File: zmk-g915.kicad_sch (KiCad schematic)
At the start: 47 parts, among them J1 Prog_conn, J2 Tag connect TC2030-CTX, J3 53047-0460, SW1 Reset Switch, U1 nRF52840-QIAA-R/nRF52833-QIAA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, U2 SN74AHCT1G125, Y1 32.768kHz, Y2 32MHz

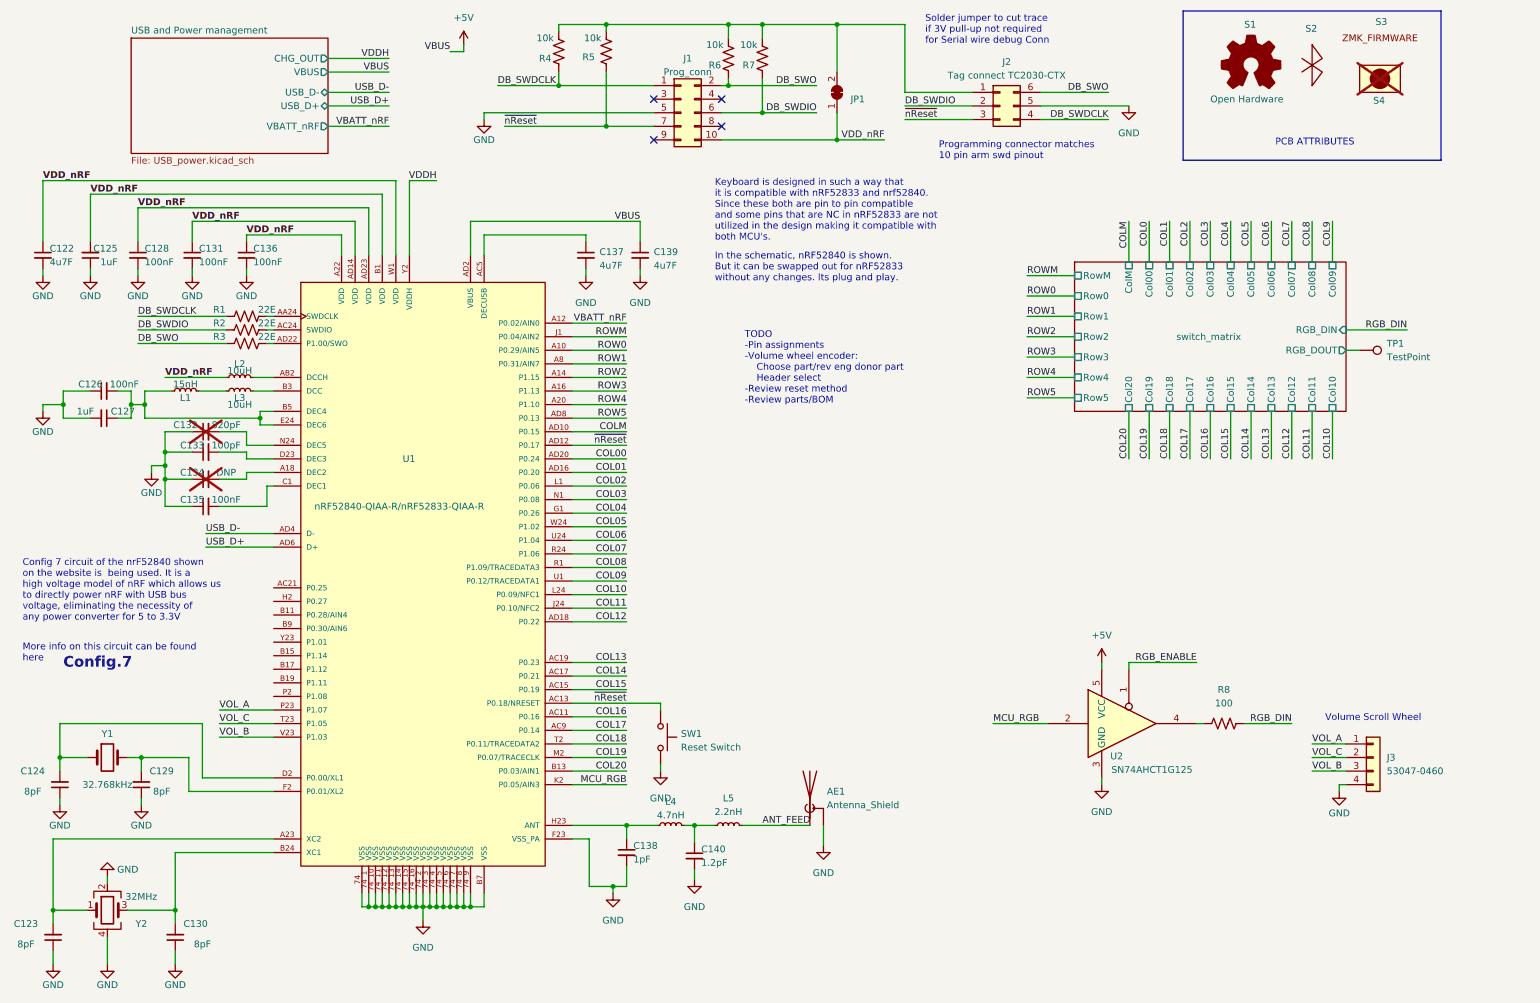
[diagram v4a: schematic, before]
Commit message: Status LEDs
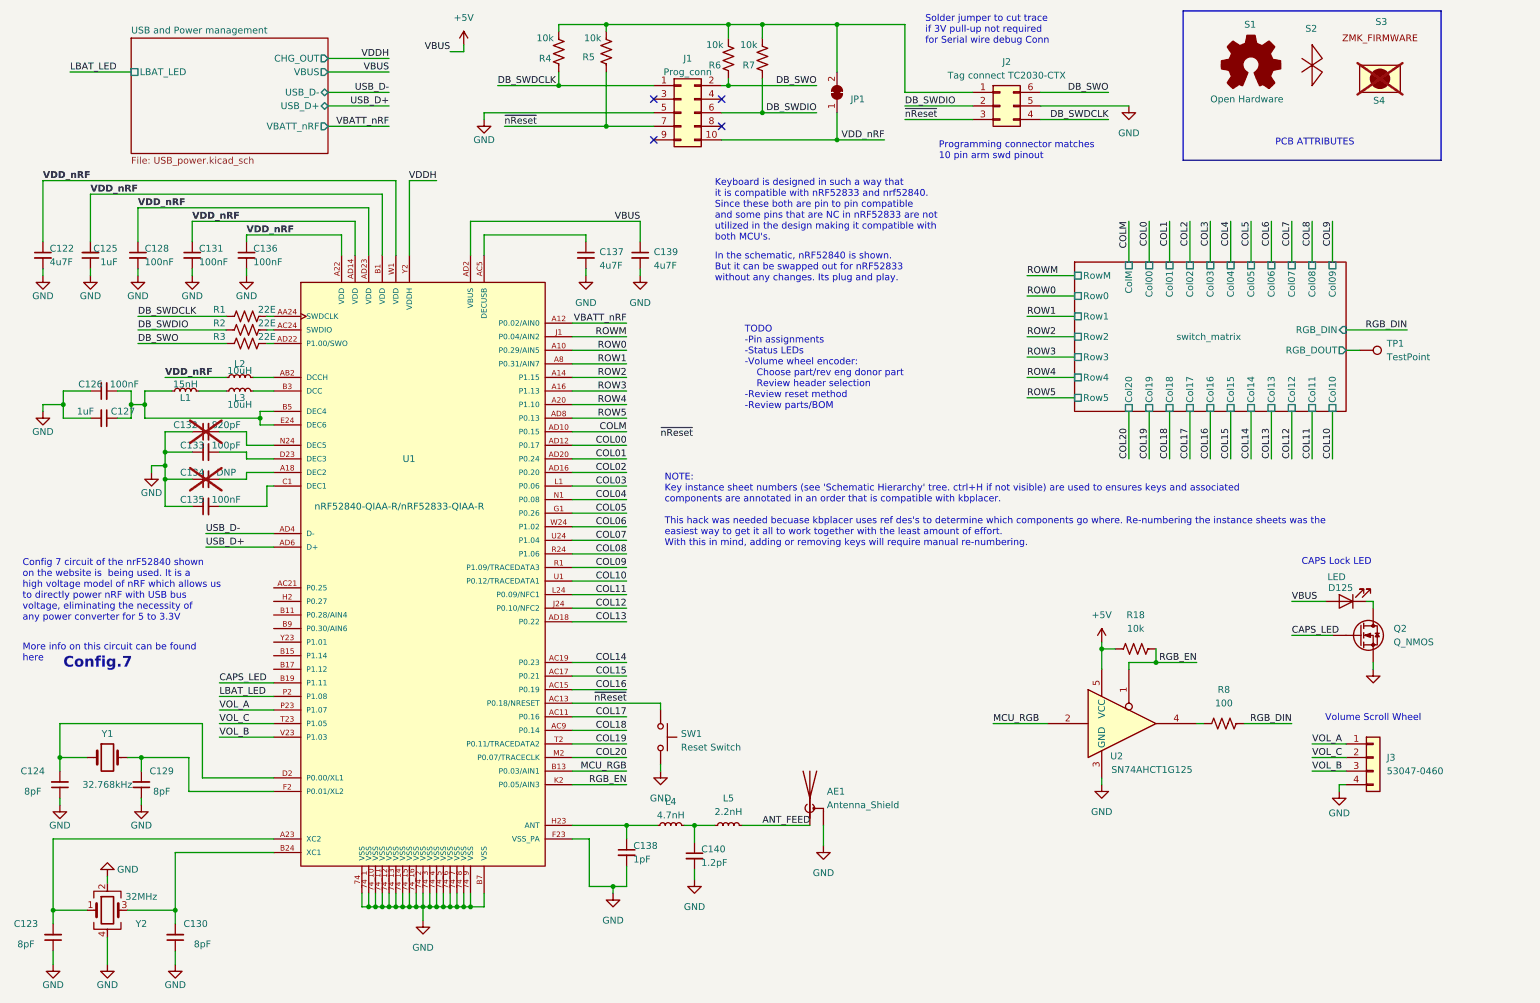
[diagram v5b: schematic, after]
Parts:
- added D125: LED, keyboard:LED_0603_1608Metric, symbol Device:LED
- added Q2: Q_NMOS, keyboard:SOT-23-3, symbol Device:Q_NMOS
- added R18: 10k, Resistor_SMD:R_0402_1005Metric, symbol keyboard:R_US
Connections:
- net +5V: now also D125.2 (A), R18.1
- net COL00: now also U1.AD12 (P0.17); no longer U1.AD20 (P0.24)
- net COL01: now also U1.AD20 (P0.24); no longer U1.AD16 (P0.20)
- net COL02: now also U1.AD16 (P0.20); no longer U1.L1 (P0.06)
- net COL03: now also U1.L1 (P0.06); no longer U1.N1 (P0.08)
- net COL04: now also U1.N1 (P0.08); no longer U1.G1 (P0.26)
- net COL05: now also U1.G1 (P0.26); no longer U1.W24 (P1.02)
- net COL06: now also U1.W24 (P1.02); no longer U1.U24 (P1.04)
- net COL07: now also U1.U24 (P1.04); no longer U1.R24 (P1.06)
- net COL08: now also U1.R24 (P1.06); no longer U1.R1 (P1.09/TRACEDATA3)
- net COL09: now also U1.R1 (P1.09/TRACEDATA3); no longer U1.U1 (P0.12/TRACEDATA1)
- net COL10: now also U1.U1 (P0.12/TRACEDATA1); no longer U1.L24 (P0.09/NFC1)
- net COL11: now also U1.L24 (P0.09/NFC1); no longer U1.J24 (P0.10/NFC2)
- net COL12: now also U1.J24 (P0.10/NFC2); no longer U1.AD18 (P0.22)
- net COL13: now also U1.AD18 (P0.22); no longer U1.AC19 (P0.23)
- net COL14: now also U1.AC19 (P0.23); no longer U1.AC17 (P0.21)
- net COL15: now also U1.AC17 (P0.21); no longer U1.AC15 (P0.19)
- net COL16: now also U1.AC15 (P0.19); no longer U1.AC11 (P0.16)
- net COL17: now also U1.AC11 (P0.16); no longer U1.AC9 (P0.14)
- net COL18: now also U1.AC9 (P0.14); no longer U1.T2 (P0.11/TRACEDATA2)
- net COL19: now also U1.T2 (P0.11/TRACEDATA2); no longer U1.M2 (P0.07/TRACECLK)
- net COL20: now also U1.M2 (P0.07/TRACECLK); no longer U1.B13 (P0.03/AIN1)
- net GND: now also Q2.S
- net MCU_RGB: now also U1.B13 (P0.03/AIN1); no longer U1.K2 (P0.05/AIN3)
- net ~{nReset}: no longer U1.AD12 (P0.17)
- net CAPS_LED: now reaches U1.B19 (P1.11)
- net CAPS_LED: now also Q2.G
- net LBAT_LED: now reaches U1.P2 (P1.08)
- net RGB_ENABLE renamed RGB_EN
- net RGB_EN: now also U1.K2 (P0.05/AIN3), R18.2
- new net: D125.1 (K), Q2.D
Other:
- sheet USB and Power management ports: added LBAT_LED; removed none
- note added: "CAPS Lock LED"
- note added: "NOTE: Key instance sheet numbers (see 'Schematic Hierarchy' tree. ctrl+H if not visible) are used to ensures keys and associated components are annotated in an order that is compatible with kbplacer. This hack was needed becuase kbplacer uses ref des's to determine which components go where. Re-numbering the instance sheets was the easiest way to get it all to work together with the least amount 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"
- note added: "TODO -Pin assignments -Status LEDs -Volume wheel encoder: Choose part/rev eng donor part Review header selection -Review reset method -Review parts/BOM"
- note removed: "TODO -Pin assignments -Volume wheel encoder: Choose part/rev eng donor part Header select -Review reset method -Review parts/BOM"

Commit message: Status LED work
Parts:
- added R20: R_US, keyboard:R_0402_1005Metric, symbol keyboard:R_US
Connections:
- net +5V: now also R20.2; no longer D125.2 (A)
- new net: D125.2 (A), R20.1
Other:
- note added: "TODO -Pin assignments -Status LEDs -Volume wheel encoder: Choose part/rev eng donor part Review header selection -Review reset necessity/method -Review parts/BOM -USB-C PD?? space dev/debug effort"
- note removed: "TODO -Pin assignments -Status LEDs -Volume wheel encoder: Choose part/rev eng donor part Review header selection -Review reset method -Review parts/BOM"
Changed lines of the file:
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@@
 		)
 	)
-	(text "TODO\n-Pin assignments\n-Status LEDs\n-Volume wheel encoder:\n	Choose part/rev eng donor part\n	Review header selection\n-Review reset method\n-Review parts/BOM"
+	(text "TODO\n-Pin assignments\n-Status LEDs\n-Volume wheel encoder:\n	Choose part/rev eng donor part\n	Review header selection\n-Review reset necessity/method\n-Review parts/BOM\n-USB-C PD??\n	space\n	dev/debug effort"
 		(exclude_from_sim no)
 		(at 151.638 80.772 0)
@@
 	(wire
 		(pts
-			(xy 254 124.46) (xy 260.35 124.46)
+			(xy 245.11 124.46) (xy 251.46 124.46)
 		)
 		(stroke
@@
 	(wire
 		(pts
+			(xy 259.08 124.46) (xy 260.35 124.46)
+		)
+		(stroke
+			(width 0)
+			(type default)
+		)
+	)
+	(wire
+		(pts
 			(xy 43.18 96.52) (xy 43.18 99.06)
 		)
@@
 	)
 	(label "VBUS"
-		(at 254 124.46 0)
+		(at 245.11 124.46 0)
 		(effects
 			(font
@@
 					(unit 1)
 				)
+			)
+		)
+	)
+	(symbol
+		(lib_id "keyboard:R_US")
+		(at 255.27 124.46 0)
+		(unit 1)
+		(exclude_from_sim no)
+		(in_bom yes)
+		(on_board yes)
+		(dnp no)
+		(property "Reference" "R20"
+			(at 255.27 121.92 0)
+			(effects
+				(font
+					(size 1.27 1.27)
+				)
+			)
+		)
+		(property "Value" "R_US"
+			(at 255.27 127 0)
+			(effects
+				(font
+					(size 1.27 1.27)
+				)
+			)
+		)
+		(property "Footprint" "keyboard:R_0402_1005Metric"
+			(at 255.016 125.476 0)
+			(effects
+				(font
+					(size 1.27 1.27)
+				)
+				(hide yes)
+			)
+		)
+		(property "Datasheet" "https://datasheet.lcsc.com/lcsc/2304140030_YAGEO-RC0402FR-071K2L_C138040.pdf"
+			(at 255.27 124.46 90)
+			(effects
+				(font
+					(size 1.27 1.27)
+				)
+				(hide yes)
+			)
+		)
+		(property "Description" ""
+			(at 255.27 124.46 0)
+			(effects
+				(font
+					(size 1.27 1.27)
+				)
+				(hide yes)
+			)
+		)
+		(property "PN" "RC0402FR-071K2L"
+			(at 255.27 124.46 0)
+			(effects
+				(font
+					(size 1.27 1.27)
+				)
+				(hide yes)
+			)
+		)
+		(property "LCSC Part Number" "C138040"
+			(at 255.27 124.46 0)
+			(effects
+				(font
+					(size 1.27 1.27)
+				)
+				(hide yes)
+			)
+		)
+		(property "LCSC link" "https://www.lcsc.com/product-detail/Chip-Resistor-Surface-Mount_YAGEO-RC0402FR-071K2L_C138040.html"
+			(at 255.27 124.46 0)
+			(effects
+				(font
+					(size 1.27 1.27)
+				)
+				(hide yes)
+			)
+		)
+		(pin "1"
+		)
+		(pin "2"
+		)
+		(instances
+			(project "zmk-g915"
+				(path "/ef112b03-6536-453f-8127-17d1495b48aa"
+					(reference "R20")
+					(unit 1)
+				)

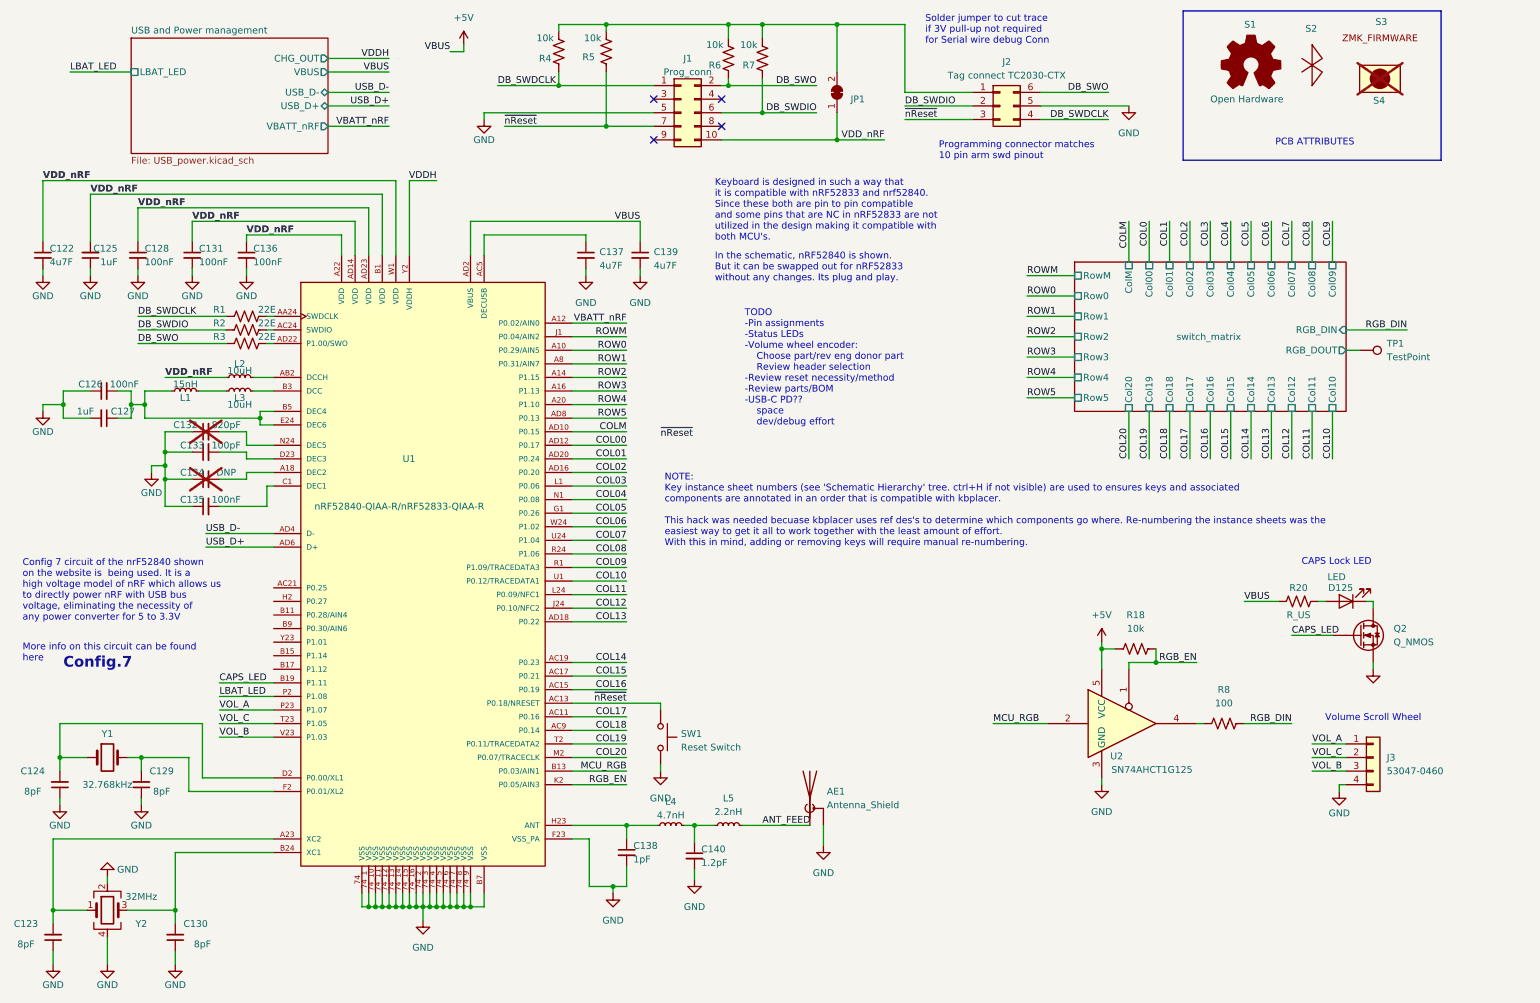
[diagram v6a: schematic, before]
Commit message: Minor sch changes. Work towards matching g915 pcb dimensions
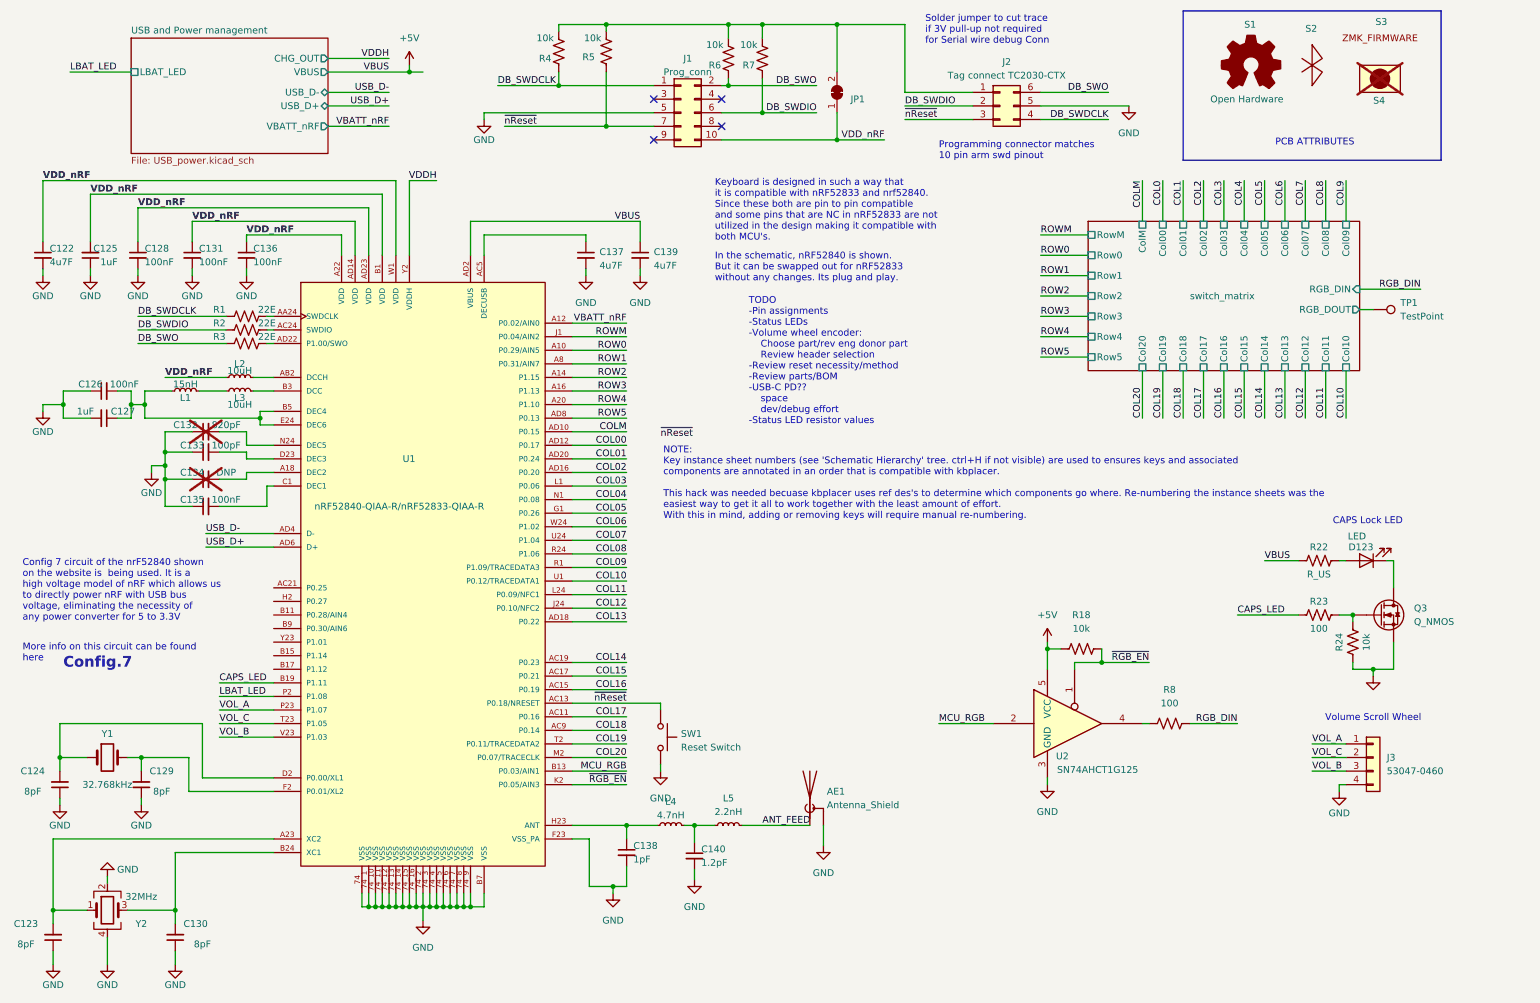
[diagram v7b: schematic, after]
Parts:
- removed D125: LED, keyboard:LED_0603_1608Metric, symbol Device:LED
- removed Q2: Q_NMOS, keyboard:SOT-23-3, symbol Device:Q_NMOS
- removed R20: R_US, keyboard:R_0402_1005Metric, symbol keyboard:R_US
- added D123: LED, keyboard:LED_0603_1608Metric, symbol Device:LED
- added Q3: Q_NMOS, keyboard:SOT-23-3, symbol Device:Q_NMOS
- added R22: R_US, keyboard:R_0402_1005Metric, symbol keyboard:R_US
- added R23: 100, keyboard:R_0402_1005Metric, symbol keyboard:R_US
- added R24: 10k, keyboard:R_0402_1005Metric, symbol keyboard:R_US
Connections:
- net +5V: now also R22.2
- net CAPS_LED: now also R23.2
- net GND: now also Q3.S, R24.2
- net RGB_EN renamed ~{RGB_EN}
- new net: Q3.G, R23.1, R24.1
- new net: D123.1 (K), Q3.D
- new net: D123.2 (A), R22.1
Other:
- note added: "TODO -Pin assignments -Status LEDs -Volume wheel encoder: Choose part/rev eng donor part Review header selection -Review reset necessity/method -Review parts/BOM -USB-C PD?? space dev/debug effort -Status LED resistor values"
- note removed: "TODO -Pin assignments -Status LEDs -Volume wheel encoder: Choose part/rev eng donor part Review header selection -Review reset necessity/method -Review parts/BOM -USB-C PD?? space dev/debug effort"
- moved on the sheet: R18, R8, TP1, U2

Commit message: Power supply and PCB stuff
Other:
- note added: "TODO -Pin assignments -Status LEDs -Volume wheel encoder: Choose part/rev eng donor part Review header selection -Review reset necessity/method -Review parts/BOM -USB-C PD?? No real benefit. Battery capcaity is low so max charging current is low. -Higher current charging IC -Status LED resistor values -Calculate max operating current consumption and review charger I termination res val"
- note removed: "TODO -Pin assignments -Status LEDs -Volume wheel encoder: Choose part/rev eng donor part Review header selection -Review reset necessity/method -Review parts/BOM -USB-C PD?? space dev/debug effort -Status LED resistor values"
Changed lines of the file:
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@@
 	(text "NOTE:\nKey instance sheet numbers (see 'Schematic Hierarchy' tree. ctrl+H if not visible) are used to ensures keys and associated\ncomponents are annotated in an order that is compatible with kbplacer.\n\nThis hack was needed becuase kbplacer uses ref des's to determine which components go where. Re-numbering the instance sheets was the\neasiest way to get it all to work together with the least amount of effort.\nWith this in mind, adding or removing keys will require manual re-numbering."
 		(exclude_from_sim no)
-		(at 136.398 102.362 0)
+		(at 136.398 104.14 0)
 		(effects
 			(font
@@
 		)
 	)
-	(text "TODO\n-Pin assignments\n-Status LEDs\n-Volume wheel encoder:\n	Choose part/rev eng donor part\n	Review header selection\n-Review reset necessity/method\n-Review parts/BOM\n-USB-C PD??\n	space\n	dev/debug effort\n-Status LED resistor values"
+	(text "TODO\n-Pin assignments\n-Status LEDs\n-Volume wheel encoder:\n	Choose part/rev eng donor part\n	Review header selection\n-Review reset necessity/method\n-Review parts/BOM\n-USB-C PD??\n	No real benefit. Battery capcaity is\n	low so max charging current is low.\n-Higher current charging IC\n-Status LED resistor values\n-Calculate max operating current consumption\n	and review charger I termination res val"
 		(exclude_from_sim no)
-		(at 152.4 79.502 0)
+		(at 151.892 81.026 0)
 		(effects
 			(font
